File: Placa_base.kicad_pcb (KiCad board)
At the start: 2 copper layers, 172 x 100 mm, 230 parts, among them J1 SWD/STLINK, J10 Interfaz con entradas digital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, J11 I2C1, J12 USART6, J13 CAN1, J14 SPI1, J15 Conn_02x08_Odd_Even, J2 Bateria, J3 Entrada 24V, J4 RS-485, J5 TV_6V, J6 AN1, J7 AN2, J8 Micro_SD_Card_Det_Hirose_DM3AT, J9 Salidas 5V, Q1 MMBT3904, Q2 MMBT3904, Q3 MMBT3904, Q4 AO3401, Q5 AO3401, SW1 SW_Push, SW2 SW_Push, SW3 SW_Push, U1 STM32F407VGTx, U10 MCP6L04T-E/ST, U11 74HCT541, U2 DC-DC_Step-Down, U3 AZ1117-3.3, U4 AZ1117-3.3, U5 RFM-0505S, U6 ISO1412, U7 WeMos_mini, U8 SIM800L_modulo, U9 Modulo_A6_Mini, Y1 32.768KHz, Y2 8MHz

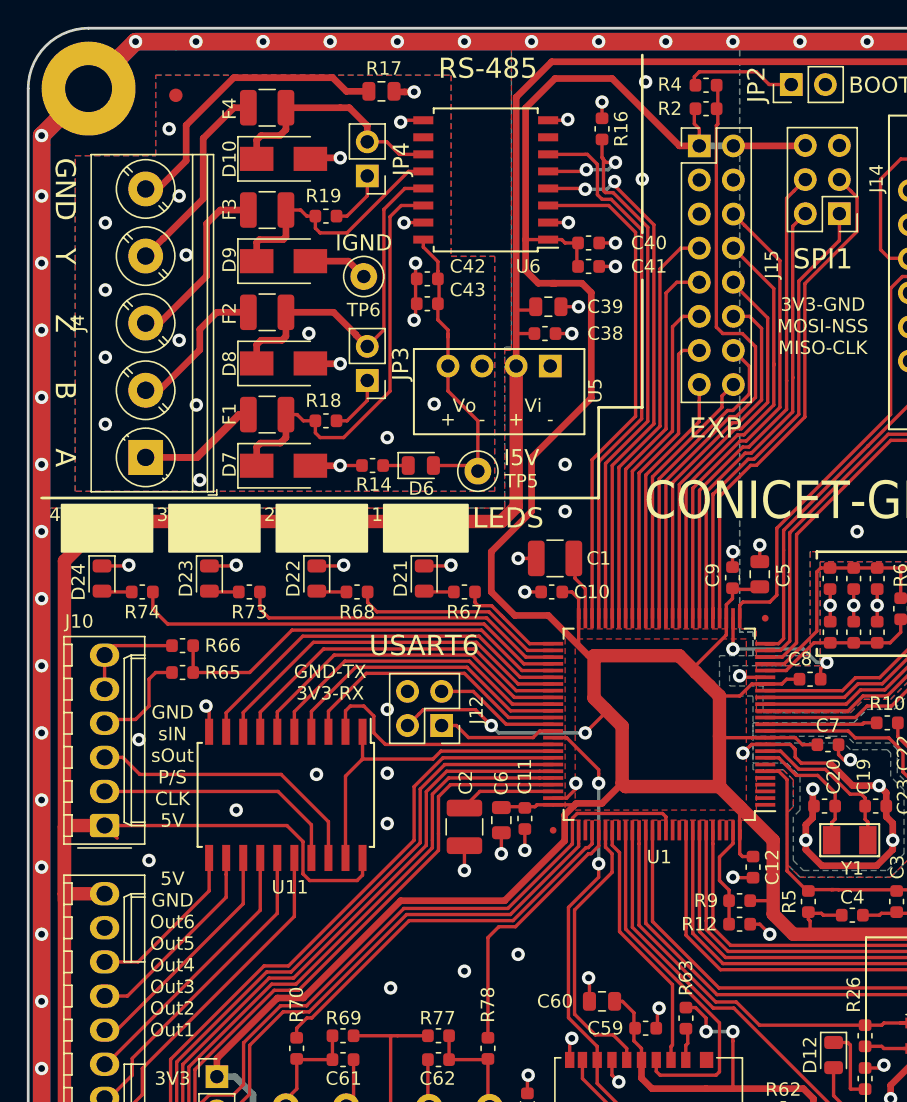
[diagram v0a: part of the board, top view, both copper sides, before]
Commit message: PCB 1.61: nombre de la placa y version
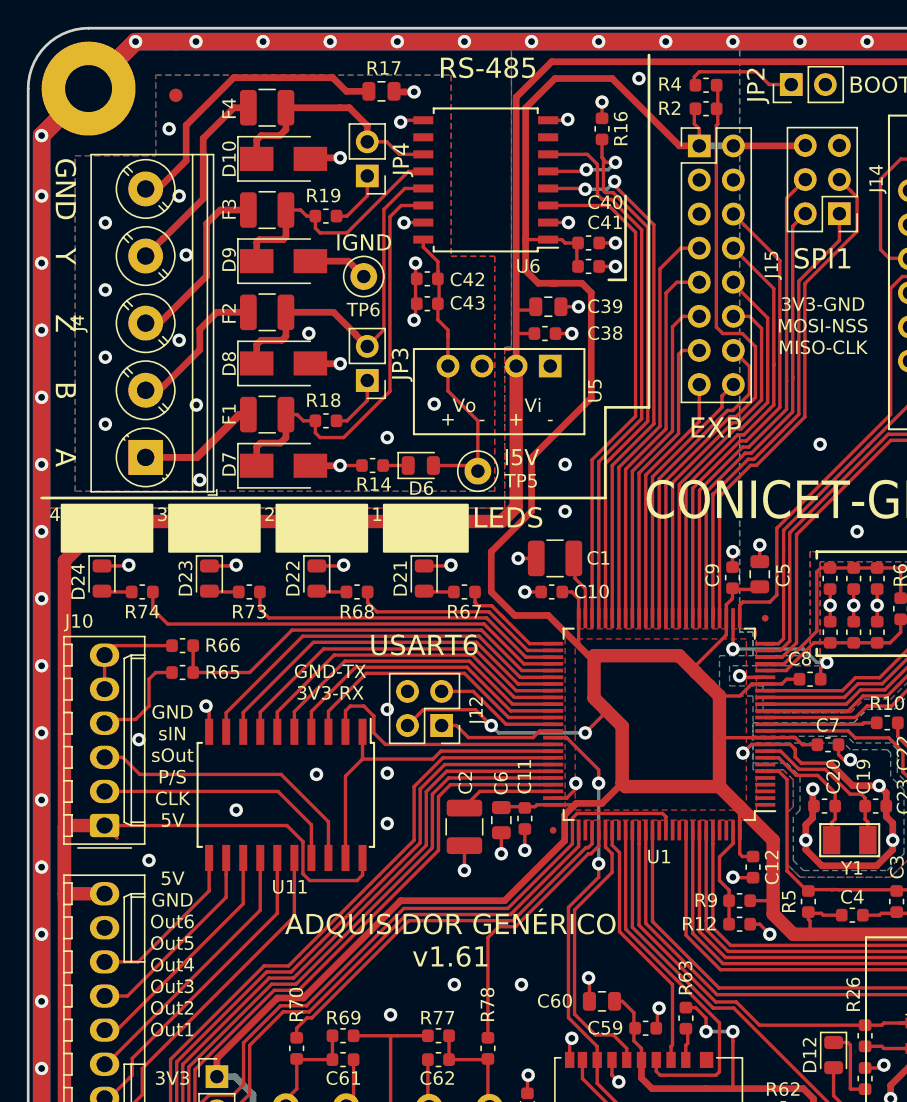
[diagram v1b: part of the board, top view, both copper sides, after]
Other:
- board text added: "ADQUISIDOR GENÉRICO v1.61"
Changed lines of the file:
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@@
   (general
     (thickness 1.6)
-    (drawings 149)
+    (drawings 151)
     (tracks 2345)
     (zones 0)
@@
   (title_block
     (title "Adquisidor genérico - Placa Base")
-    (date 2019-08-02)
-    (rev V1.6)
+    (date 2019-08-04)
+    (rev V1.61)
     (company "Trenes Argentinos Operaciones")
     (comment 1 "Colaboradores: Santiago Germino")
@@
     (tags capacitor)
     (attr smd)
-    (fp_text reference C43 (at -3.015 1.028 180) (layer F.SilkS)
+    (fp_text reference C43 (at -3.015 0.028 180) (layer F.SilkS)
       (effects (font (size 1 1) (thickness 0.15)))
     )
@@
     (tags capacitor)
     (attr smd)
-    (fp_text reference C42 (at -3.015 0.924 180) (layer F.SilkS)
+    (fp_text reference C42 (at -3.015 -0.076 180) (layer F.SilkS)
       (effects (font (size 1 1) (thickness 0.15)))
     )
@@
     (tags capacitor)
     (attr smd)
-    (fp_text reference C41 (at 4.5 0) (layer F.SilkS)
+    (fp_text reference C41 (at 1.25 -3.25) (layer F.SilkS)
       (effects (font (size 1 1) (thickness 0.15)))
     )
@@
     (tags capacitor)
     (attr smd)
-    (fp_text reference C40 (at 4.5 0) (layer F.SilkS)
+    (fp_text reference C40 (at 1.25 -3) (layer F.SilkS)
       (effects (font (size 1 1) (thickness 0.15)))
     )
@@
       (xy -0.318963 -2.21964)) (layer F.SilkS) (width 0.01))
   )
+  (gr_text "ADQUISIDOR GENÉRICO\nv1.61" (at 101.5 108) (layer F.SilkS)
+    (effects (font (size 1.5 1.5) (thickness 0.3)))
+  )
+  (gr_line (start 114.5 58.75) (end 113.25 58.75) (layer F.SilkS) (width 0.2))
+  (gr_line (start 114.5 52.5) (end 114.5 58.75) (layer F.SilkS) (width 0.2))
   (gr_line (start 210.6 64) (end 211.7 64) (layer F.SilkS) (width 0.2))
   (gr_line (start 211.7 64) (end 211.7 63.7) (layer F.SilkS) (width 0.2))
@@
     (arrow2b (pts (xy 237.5 29) (xy 236.373496 29.586421)))
   )
-  (gr_line (start 115.75 68.25) (end 115.75 58.75) (layer F.SilkS) (width 0.2))
-  (gr_line (start 112.5 68.25) (end 115.75 68.25) (layer F.SilkS) (width 0.2))
-  (gr_line (start 112.5 75) (end 112.5 68.25) (layer F.SilkS) (width 0.2))
+  (gr_line (start 113 68.25) (end 116.25 68.25) (layer F.SilkS) (width 0.2))
+  (gr_line (start 113 75) (end 113 68.25) (layer F.SilkS) (width 0.2))
   (gr_text PWR (at 239.25 124.75 90) (layer F.SilkS)
     (effects (font (size 1.5 1.5) (thickness 0.3)))
@@
   (gr_line (start 204.5 90) (end 204.5 85.75) (layer F.SilkS) (width 0.2))
   (gr_line (start 240 90) (end 204.5 90) (layer F.SilkS) (width 0.2))
-  (gr_line (start 115.75 55.25) (end 115.75 42) (layer F.SilkS) (width 0.2))
-  (gr_line (start 71 75) (end 112.5 75) (layer F.SilkS) (width 0.2))
+  (gr_line (start 116.25 68.25) (end 116.25 42) (layer F.SilkS) (width 0.2))
+  (gr_line (start 71 75) (end 113 75) (layer F.SilkS) (width 0.2))
   (gr_text GND (at 72.75 52 270) (layer F.SilkS)
     (effects (font (size 1.5 1.5) (thickness 0.3)))
@@
   (via (at 116.5 129) (size 1) (drill 0.5) (layers F.Cu B.Cu) (net 6))
   (via (at 79 102) (size 1) (drill 0.5) (layers F.Cu B.Cu) (net 6))
-  (via (at 97 111.5) (size 1) (drill 0.5) (layers F.Cu B.Cu) (net 6))
+  (via (at 97 113.5) (size 1) (drill 0.5) (layers F.Cu B.Cu) (net 6))
   (via (at 110 72.5) (size 1) (drill 0.5) (layers F.Cu B.Cu) (net 6))
   (via (at 110 76) (size 1) (drill 0.5) (layers F.Cu B.Cu) (net 6))
@@
   (via (at 149.334 52.316) (size 1) (drill 0.5) (layers F.Cu B.Cu) (net 6))
   (via (at 144.508 52.316) (size 1) (drill 0.5) (layers F.Cu B.Cu) (net 6))
-  (via (at 115.75 51.25) (size 1) (drill 0.5) (layers F.Cu B.Cu) (net 6))
-  (via (at 106.5 109) (size 1) (drill 0.5) (layers F.Cu B.Cu) (net 6))
+  (via (at 129 71) (size 1) (drill 0.5) (layers F.Cu B.Cu) (net 6))
+  (via (at 106.75 111.25) (size 1) (drill 0.5) (layers F.Cu B.Cu) (net 6))
   (via (at 141.75 113.75) (size 1) (drill 0.5) (layers F.Cu B.Cu) (net 6))
   (via (at 163.5 129.25) (size 1) (drill 0.5) (layers F.Cu B.Cu) (net 6))
@@
   (via (at 200.5 88.5) (size 1) (drill 0.5) (layers F.Cu B.Cu) (net 6))
   (via (at 165.75 106.75) (size 1) (drill 0.5) (layers F.Cu B.Cu) (net 6))
-  (via (at 116 44) (size 1) (drill 0.5) (layers F.Cu B.Cu) (net 6))
-  (via (at 102.5 110.25) (size 1) (drill 0.5) (layers F.Cu B.Cu) (net 6))
+  (via (at 115.5 43.75) (size 1) (drill 0.5) (layers F.Cu B.Cu) (net 6))
+  (via (at 101.75 111.25) (size 1) (drill 0.5) (layers F.Cu B.Cu) (net 6))
   (via (at 78.25 93) (size 1) (drill 0.5) (layers F.Cu B.Cu) (net 6))
   (via (at 111 60.75) (size 1) (drill 0.5) (layers F.Cu B.Cu) (net 6))

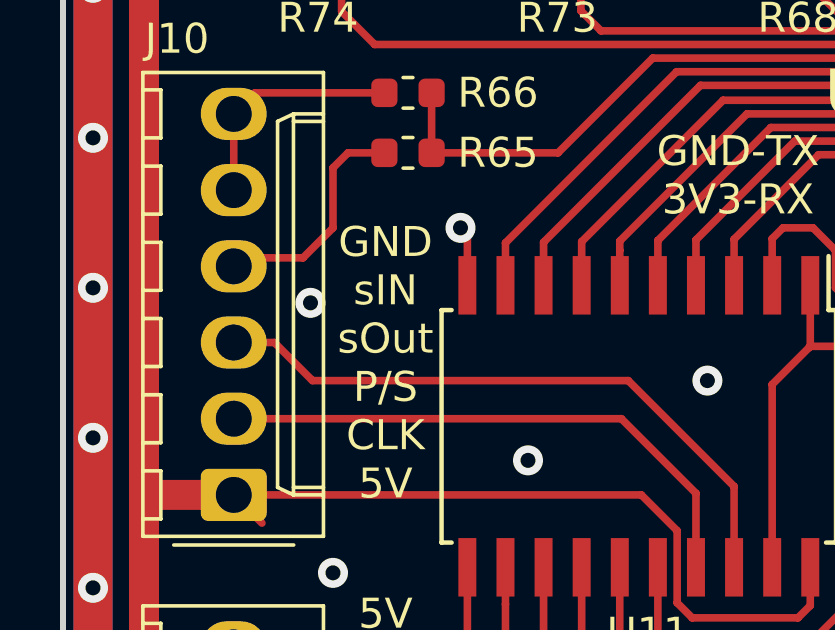
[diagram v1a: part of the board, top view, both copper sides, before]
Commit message: PCB 1.62: serigrafía pines J10
Actualización de PDF y cambios mínimos.
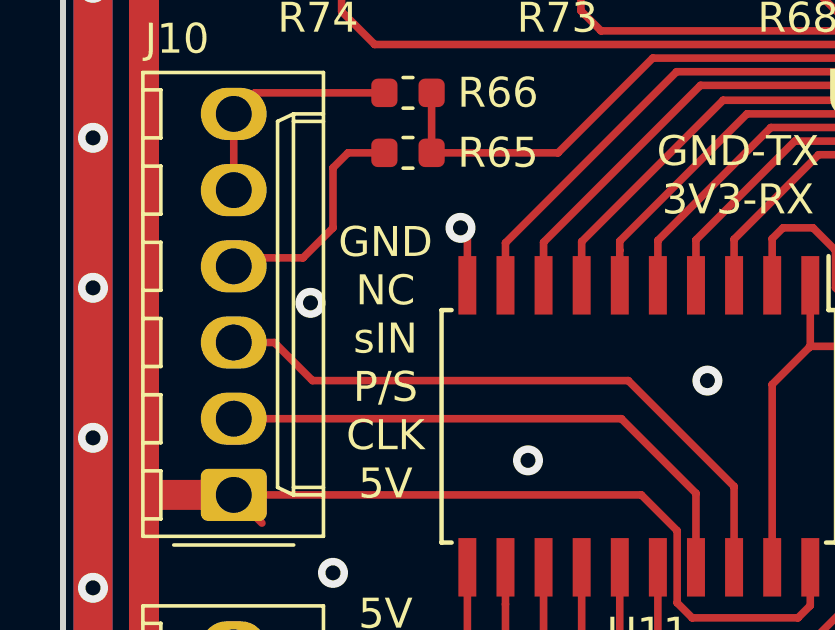
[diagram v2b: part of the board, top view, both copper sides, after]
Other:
- board text added: "GND NC sIN P/S CLK 5V"
- board text removed: "GND sIN sOut P/S CLK 5V"
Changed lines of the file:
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@@
-(kicad_pcb (version 20171130) (host pcbnew 5.0.2+dfsg1-1~bpo9+1)
+(kicad_pcb (version 20171130) (host pcbnew "(5.0.2)-1")
   (general
     (thickness 1.6)
@@
   (title_block
     (title "Adquisidor genérico - Placa Base")
-    (date 2019-08-04)
-    (rev V1.61)
+    (date 2019-08-06)
+    (rev V1.62)
     (company "Trenes Argentinos Operaciones")
     (comment 1 "Colaboradores: Santiago Germino")
@@
     (effects (font (size 1 1) (thickness 0.15)))
   )
-  (gr_text "GND\nsIN\nsOut\nP/S\nCLK\n5V" (at 80.75 95) (layer F.SilkS)
+  (gr_text "GND\nNC\nsIN\nP/S\nCLK\n5V" (at 80.75 95) (layer F.SilkS)
     (effects (font (size 1 1) (thickness 0.15)))
   )

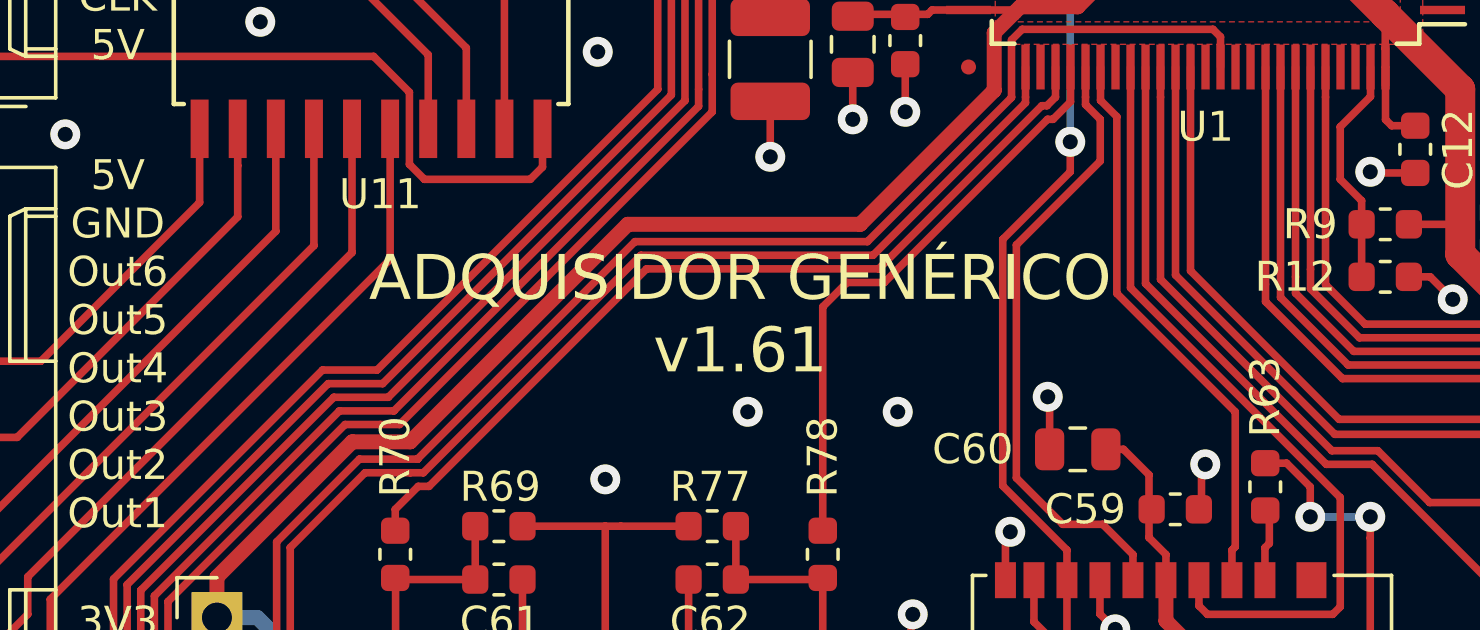
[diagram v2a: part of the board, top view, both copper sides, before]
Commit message: PCB v1.62: Cambio de nombre
Cambio de nombre a Módulo de procesamiento y versión a v1.62.
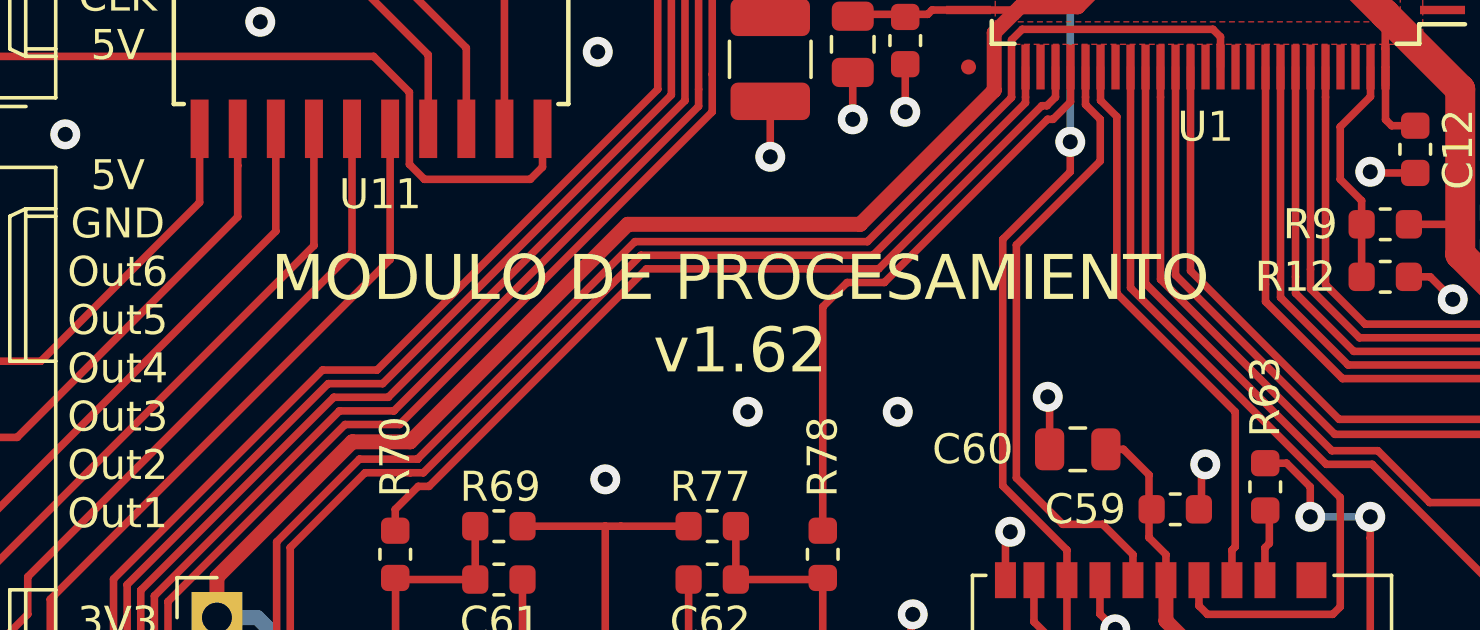
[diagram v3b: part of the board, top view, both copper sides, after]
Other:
- board text added: "MODULO DE PROCESAMIENTO v1.62"
- board text removed: "ADQUISIDOR GENÉRICO v1.61"
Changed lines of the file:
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@@
       (xy -0.318963 -2.21964)) (layer F.SilkS) (width 0.01))
   )
-  (gr_text "ADQUISIDOR GENÉRICO\nv1.61" (at 101.5 108) (layer F.SilkS)
+  (gr_text "MODULO DE PROCESAMIENTO\nv1.62" (at 101.5 108) (layer F.SilkS)
     (effects (font (size 1.5 1.5) (thickness 0.3)))
   )
